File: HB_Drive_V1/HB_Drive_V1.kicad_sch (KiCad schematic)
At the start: 0 parts

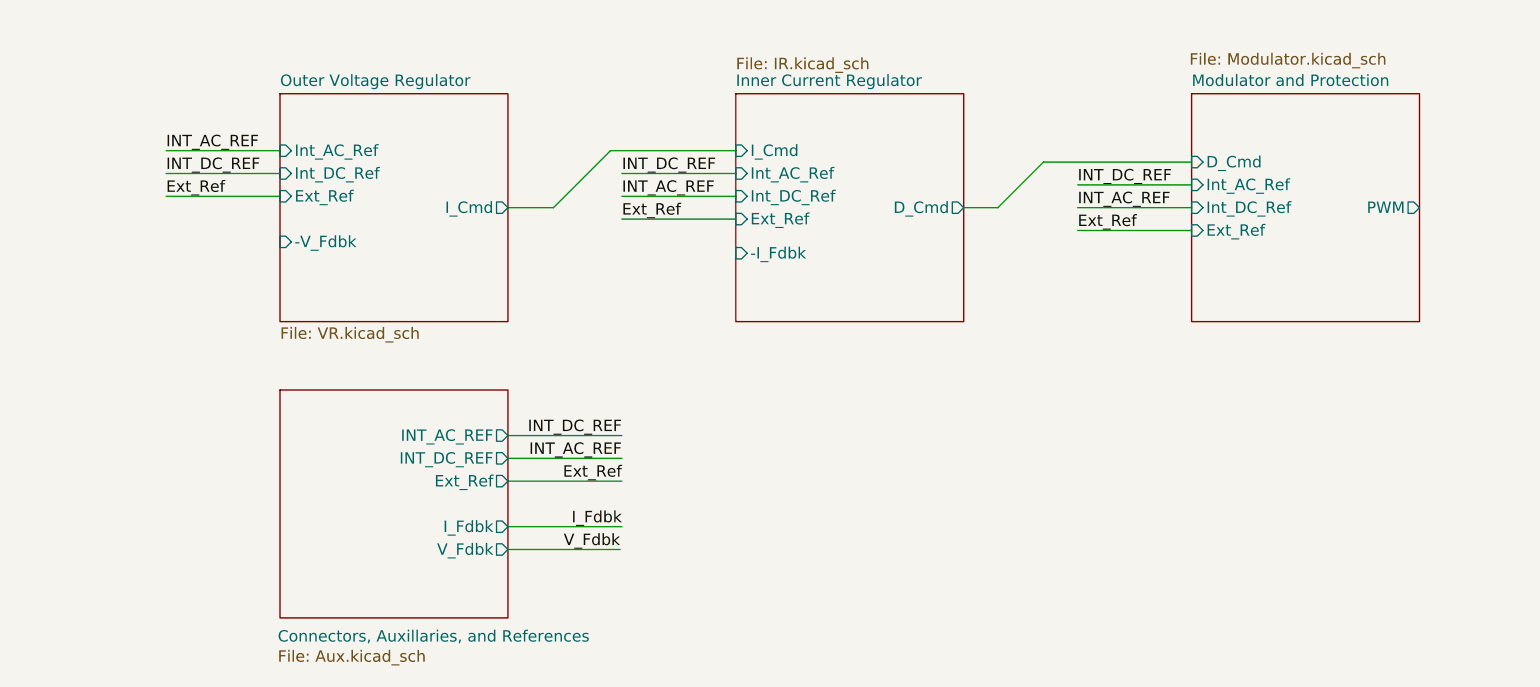
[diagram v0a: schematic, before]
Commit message: finishes hirearchical labels, add 10v +- ref generation and updates the DC offset circuits
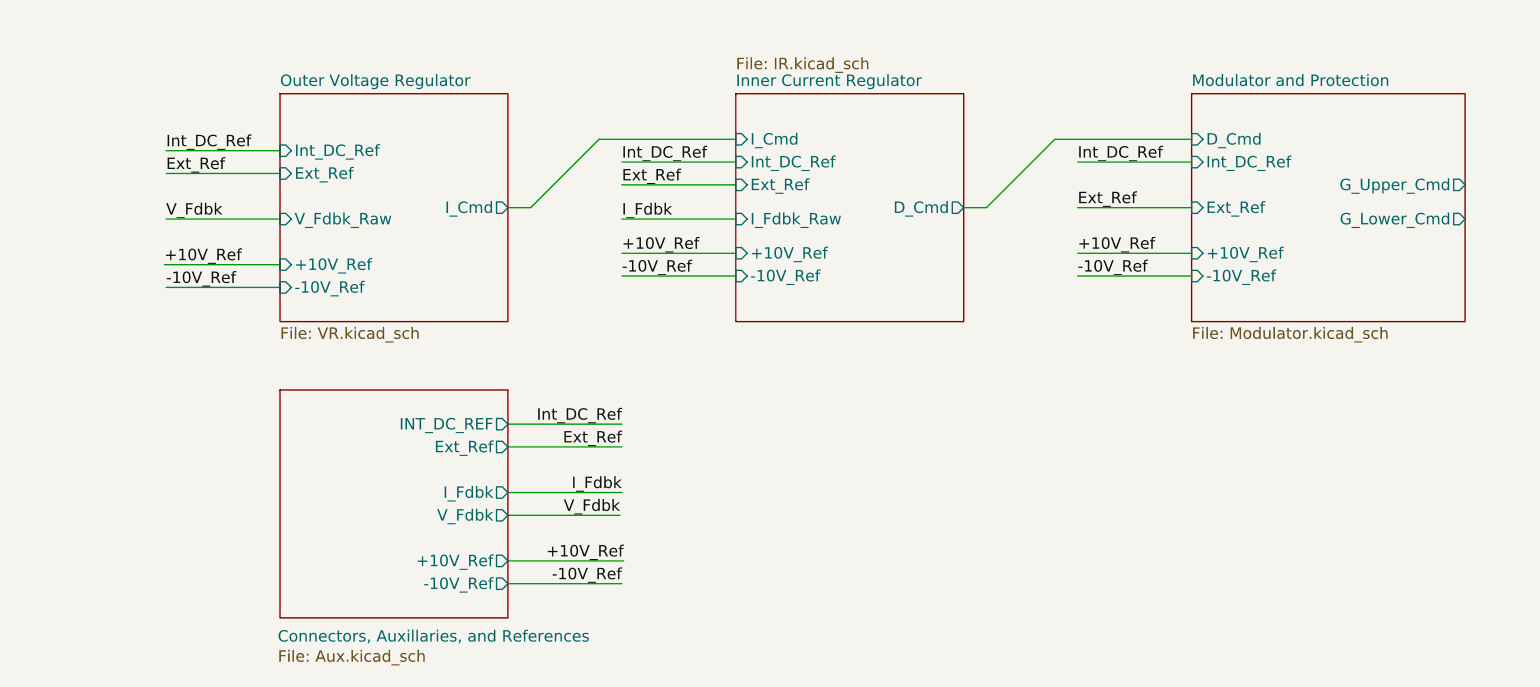
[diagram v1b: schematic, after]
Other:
- sheet Connectors, Auxillaries, and References ports: added +10V_Ref, -10V_Ref; removed INT_AC_REF
- sheet Inner Current Regulator ports: added +10V_Ref, -10V_Ref, I_Fdbk_Raw; removed -I_Fdbk, Int_AC_Ref
- sheet Modulator and Protection ports: added +10V_Ref, -10V_Ref, G_Lower_Cmd, G_Upper_Cmd; removed Int_AC_Ref, PWM
- sheet Outer Voltage Regulator ports: added +10V_Ref, -10V_Ref, V_Fdbk_Raw; removed -V_Fdbk, Int_AC_Ref

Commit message: updates board to highest working copy
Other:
- sheet Connectors, Auxillaries, and References ports: added Ext_Cmd, G_Lower_Cmd, G_Upper_Cmd, I_Fdbk_Raw, Int_Cmd, V_Fdbk_Raw; removed Ext_Ref, INT_DC_REF, I_Fdbk, V_Fdbk
- sheet Inner Current Regulator ports: added Ext_Cmd, Int_Cmd; removed Ext_Ref, Int_DC_Ref
- sheet Modulator and Protection ports: added Ext_Cmd, I_Fdbk_Raw, Int_Cmd; removed Ext_Ref, Int_DC_Ref
- sheet Outer Voltage Regulator ports: added Ext_Cmd, Int_Cmd; removed Ext_Ref, Int_DC_Ref

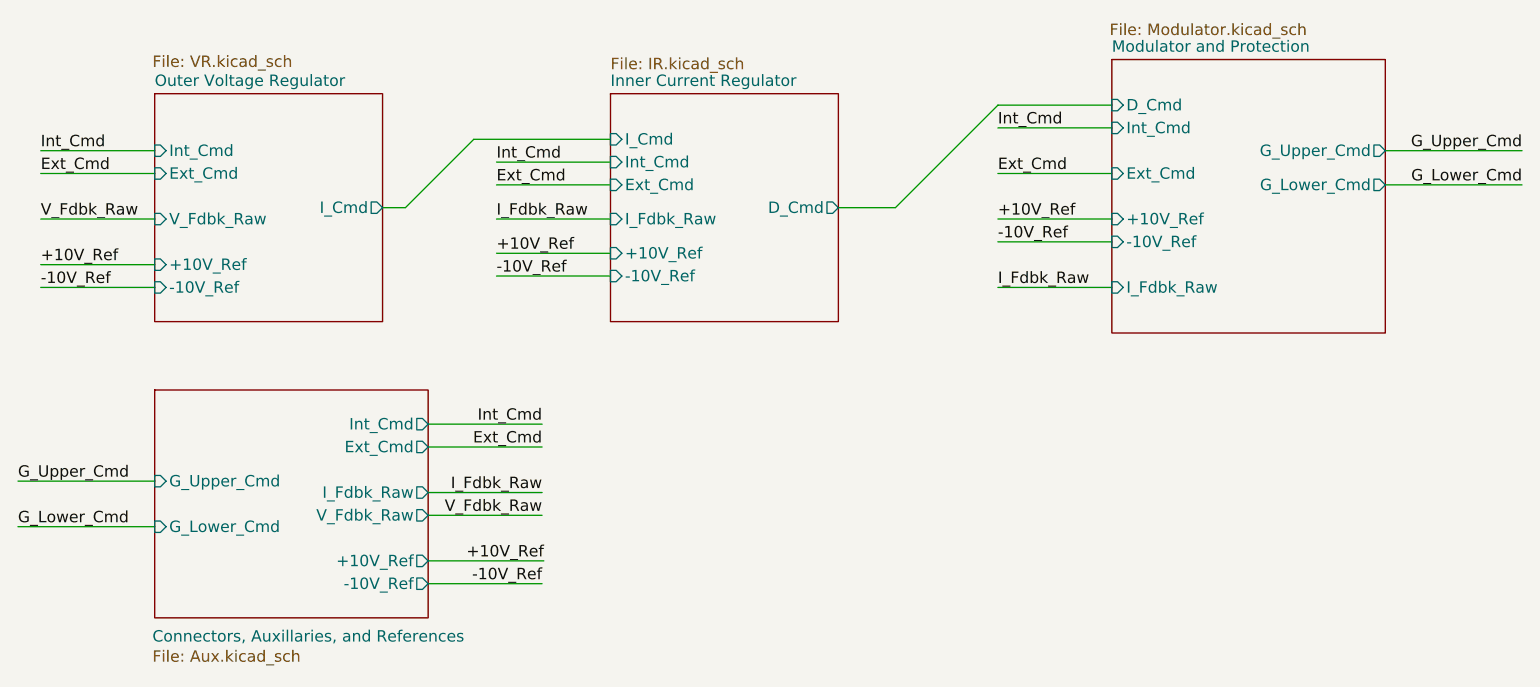
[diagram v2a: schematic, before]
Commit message: removes Aux file trouble
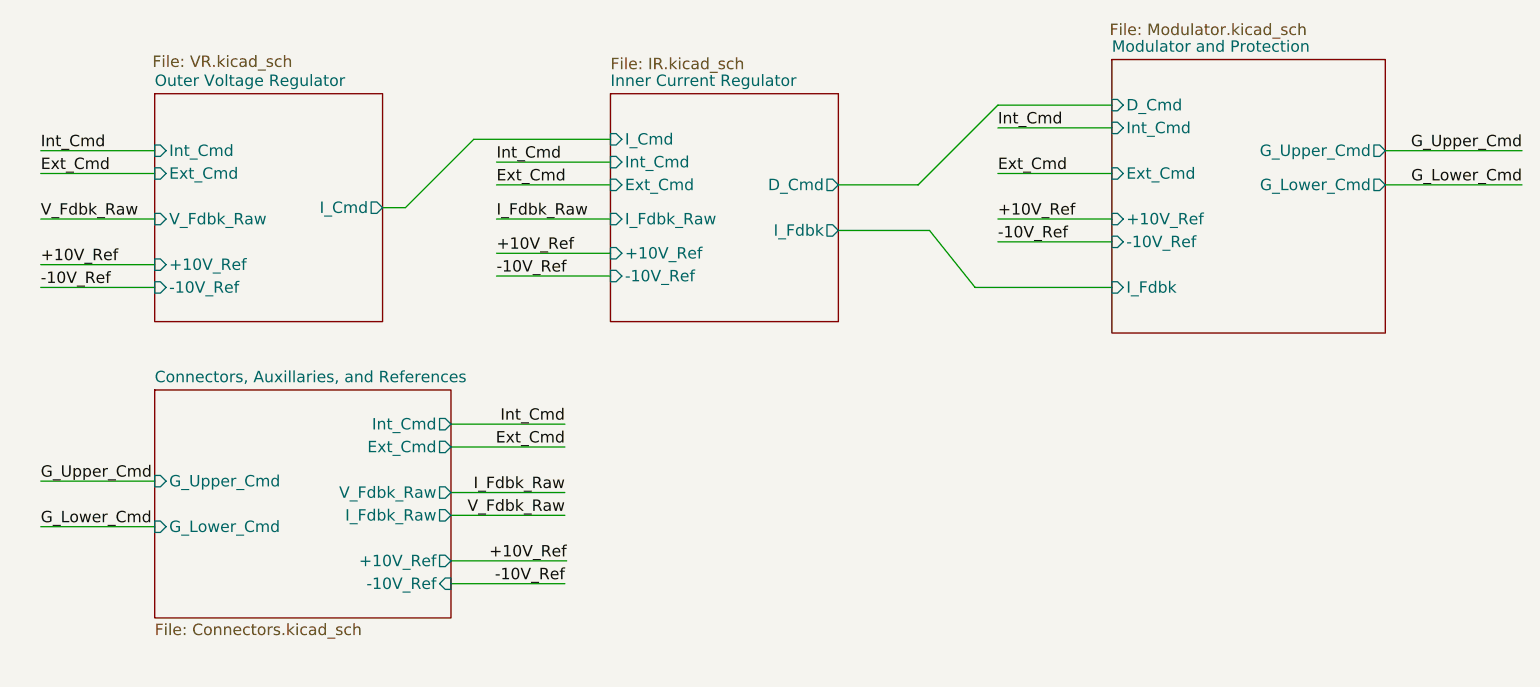
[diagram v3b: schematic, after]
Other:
- sheet Connectors, Auxillaries, and References: file Aux.kicad_sch -> Connectors.kicad_sch
- sheet Inner Current Regulator ports: added I_Fdbk; removed none
- sheet Modulator and Protection ports: added I_Fdbk; removed I_Fdbk_Raw
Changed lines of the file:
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@@
 	(wire
 		(pts
-			(xy 105.41 123.19) (xy 118.11 123.19)
-		)
-		(stroke
-			(width 0)
-			(type default)
-		)
-	)
-	(wire
-		(pts
-			(xy 105.41 115.57) (xy 118.11 115.57)
-		)
-		(stroke
-			(width 0)
-			(type default)
-		)
-	)
-	(wire
-		(pts
-			(xy 118.11 113.03) (xy 105.41 113.03)
-		)
-		(stroke
-			(width 0)
-			(type default)
-		)
-	)
-	(wire
-		(pts
-			(xy 59.69 111.76) (xy 74.93 111.76)
+			(xy 107.95 123.19) (xy 120.65 123.19)
+		)
+		(stroke
+			(width 0)
+			(type default)
+		)
+	)
+	(wire
+		(pts
+			(xy 107.95 115.57) (xy 120.65 115.57)
+		)
+		(stroke
+			(width 0)
+			(type default)
+		)
+	)
+	(wire
+		(pts
+			(xy 120.65 113.03) (xy 107.95 113.03)
+		)
+		(stroke
+			(width 0)
+			(type default)
+		)
+	)
+	(wire
+		(pts
+			(xy 62.23 111.76) (xy 74.93 111.76)
 		)
 		(stroke
@@
 	(wire
 		(pts
+			(xy 166.37 90.17) (xy 161.29 83.82)
+		)
+		(stroke
+			(width 0)
+			(type default)
+		)
+	)
+	(wire
+		(pts
+			(xy 151.13 83.82) (xy 161.29 83.82)
+		)
+		(stroke
+			(width 0)
+			(type default)
+		)
+	)
+	(wire
+		(pts
 			(xy 168.91 69.85) (xy 181.61 69.85)
 		)
@@
 	(wire
 		(pts
-			(xy 59.69 116.84) (xy 74.93 116.84)
+			(xy 62.23 116.84) (xy 74.93 116.84)
+		)
+		(stroke
+			(width 0)
+			(type default)
+		)
+	)
+	(wire
+		(pts
+			(xy 151.13 78.74) (xy 160.02 78.74)
 		)
 		(stroke
@@
 	(wire
 		(pts
-			(xy 118.11 105.41) (xy 105.41 105.41)
-		)
-		(stroke
-			(width 0)
-			(type default)
-		)
-	)
-	(wire
-		(pts
-			(xy 151.13 81.28) (xy 157.48 81.28)
+			(xy 120.65 105.41) (xy 107.95 105.41)
+		)
+		(stroke
+			(width 0)
+			(type default)
+		)
+	)
+	(wire
+		(pts
+			(xy 181.61 90.17) (xy 166.37 90.17)
 		)
 		(stroke
@@
 	(wire
 		(pts
-			(xy 105.41 120.65) (xy 118.308 120.65)
+			(xy 107.95 120.65) (xy 120.848 120.65)
 		)
 		(stroke
@@
 	(wire
 		(pts
-			(xy 157.48 81.28) (xy 168.91 69.85)
-		)
-		(stroke
-			(width 0)
-			(type default)
-		)
-	)
-	(wire
-		(pts
-			(xy 118.11 107.95) (xy 105.41 107.95)
-		)
-		(stroke
-			(width 0)
-			(type default)
-		)
-	)
-	(wire
-		(pts
-			(xy 168.91 90.17) (xy 181.61 90.17)
+			(xy 160.02 78.74) (xy 168.91 69.85)
+		)
+		(stroke
+			(width 0)
+			(type default)
+		)
+	)
+	(wire
+		(pts
+			(xy 120.65 107.95) (xy 107.95 107.95)
 		)
 		(stroke
@@
 	)
 	(label "V_Fdbk_Raw"
-		(at 118.11 115.57 180)
+		(at 120.65 115.57 180)
 		(effects
 			(font
@@
 	)
 	(label "G_Lower_Cmd"
-		(at 59.69 116.84 0)
+		(at 62.23 116.84 0)
 		(effects
 			(font
@@
 	)
 	(label "-10V_Ref"
-		(at 118.11 123.19 180)
+		(at 120.65 123.19 180)
 		(effects
 			(font
@@
 			)
 			(justify right bottom)
-		)
-	)
-	(label "I_Fdbk_Raw"
-		(at 168.91 90.17 0)
-		(effects
-			(font
-				(size 1.27 1.27)
-			)
-			(justify left bottom)
 		)
 	)
@@
 	)
 	(label "Int_Cmd"
-		(at 118.11 105.41 180)
+		(at 120.65 105.41 180)
 		(effects
 			(font
@@
 	)
 	(label "G_Upper_Cmd"
-		(at 59.69 111.76 0)
+		(at 62.23 111.76 0)
 		(effects
 			(font
@@
 	)
 	(label "+10V_Ref"
-		(at 118.308 120.65 180)
+		(at 120.848 120.65 180)
 		(effects
 			(font
@@
 	)
 	(label "I_Fdbk_Raw"
-		(at 118.11 113.03 180)
+		(at 120.65 113.03 180)
 		(effects
 			(font
@@
 	)
 	(label "Ext_Cmd"
-		(at 118.11 107.95 180)
+		(at 120.65 107.95 180)
 		(effects
 			(font
@@
 			)
 		)
-		(pin "I_Fdbk_Raw" input
+		(pin "I_Fdbk" input
 			(at 181.61 90.17 180)
 			(effects
@@
 		)
 		(pin "D_Cmd" output
-			(at 151.13 81.28 0)
+			(at 151.13 78.74 0)
 			(effects
 				(font
@@
 				)
 				(justify left)
+			)
+		)
+		(pin "I_Fdbk" output
+			(at 151.13 83.82 0)
+			(effects
+				(font
+					(size 1.27 1.27)
+				)
+				(justify right)
 			)
 		)
@@
 	(sheet
 		(at 74.93 101.6)
-		(size 30.48 25.4)
+		(size 33.02 25.4)
 		(exclude_from_sim no)
 		(in_bom yes)
 		(on_board yes)
 		(dnp no)
+		(fields_autoplaced yes)
 		(stroke
 			(width 0.1524)
@@
 		)
 		(property "Sheetname" "Connectors, Auxillaries, and References"
-			(at 74.676 129.794 0)
+			(at 74.93 100.8884 0)
 			(show_name no)
 			(do_not_autoplace no)
@@
 			)
 		)
-		(property "Sheetfile" "Aux.kicad_sch"
-			(at 74.676 130.556 0)
+		(property "Sheetfile" "Connectors.kicad_sch"
+			(at 74.93 127.5846 0)
 			(show_name no)
 			(do_not_autoplace no)
@@
 			)
 		)
+		(pin "+10V_Ref" output
+			(at 107.95 120.65 0)
+			(effects
+				(font
+					(size 1.27 1.27)
+				)
+				(justify right)
+			)
+		)
+		(pin "-10V_Ref" input
+			(at 107.95 123.19 0)
+			(effects
+				(font
+					(size 1.27 1.27)
+				)
+				(justify right)
+			)
+		)
 		(pin "Ext_Cmd" output
-			(at 105.41 107.95 0)
-			(effects
-				(font
-					(size 1.27 1.27)
-				)
-				(justify right)
-			)
-		)
-		(pin "+10V_Ref" output
-			(at 105.41 120.65 0)
-			(effects
-				(font
-					(size 1.27 1.27)
-				)
-				(justify right)
-			)
-		)
-		(pin "-10V_Ref" output
-			(at 105.41 123.19 0)
-			(effects
-				(font
-					(size 1.27 1.27)
-				)
-				(justify right)
-			)
-		)
-		(pin "I_Fdbk_Raw" output
-			(at 105.41 113.03 0)
-			(effects
-				(font
-					(size 1.27 1.27)
-				)
-				(justify right)
-			)
-		)
-		(pin "V_Fdbk_Raw" output
-			(at 105.41 115.57 0)
+			(at 107.95 107.95 0)
 			(effects
 				(font
@@
 		)
 		(pin "Int_Cmd" output
-			(at 105.41 105.41 0)
+			(at 107.95 105.41 0)
+			(effects
+				(font
+					(size 1.27 1.27)
+				)
+				(justify right)
+			)
+		)
+		(pin "I_Fdbk_Raw" output
+			(at 107.95 115.57 0)
+			(effects
+				(font
+					(size 1.27 1.27)
+				)
+				(justify right)
+			)
+		)
+		(pin "V_Fdbk_Raw" output
+			(at 107.95 113.03 0)
 			(effects
 				(font
@@
 			(project "HB_Drive_V1"
 				(path "/a9b54c89-4c8e-4c90-8a0d-ec2009e369b7"
-					(page "9")
-				)
-			)
+					(page "5")
+				)
+			)

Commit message: Annotates Schematic! Fixes REV1 wiring swaps and replaces buffer
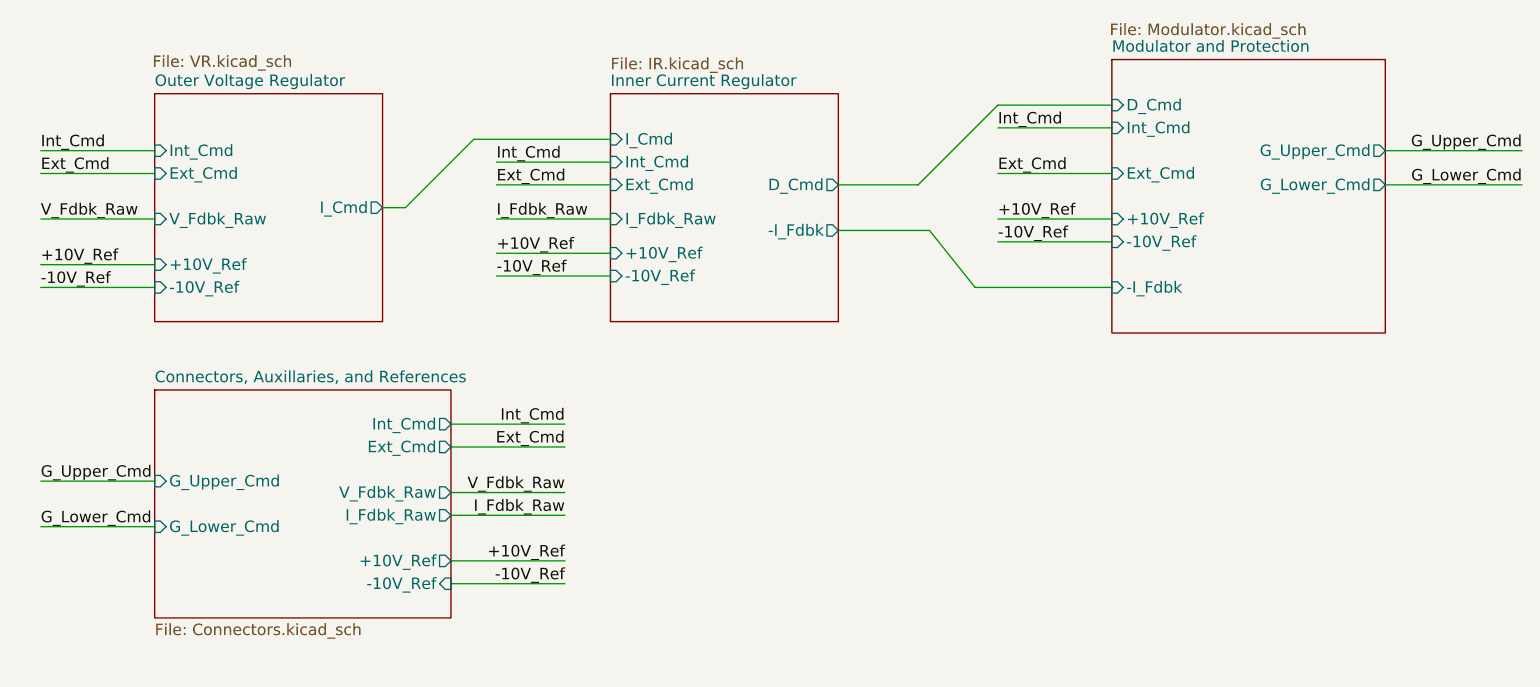
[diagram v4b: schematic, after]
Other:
- sheet Inner Current Regulator ports: added -I_Fdbk; removed I_Fdbk
- sheet Modulator and Protection ports: added -I_Fdbk; removed I_Fdbk
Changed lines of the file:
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@@
 	(wire
 		(pts
-			(xy 107.95 120.65) (xy 120.848 120.65)
+			(xy 107.95 120.65) (xy 120.65 120.65)
 		)
 		(stroke
@@
 			(width 0)
 			(type default)
-		)
-	)
-	(label "V_Fdbk_Raw"
-		(at 120.65 115.57 180)
-		(effects
-			(font
-				(size 1.27 1.27)
-			)
-			(justify right bottom)
 		)
 	)
@@
 		)
 	)
+	(label "V_Fdbk_Raw"
+		(at 120.65 113.03 180)
+		(effects
+			(font
+				(size 1.27 1.27)
+			)
+			(justify right bottom)
+		)
+	)
 	(label "-10V_Ref"
 		(at 120.65 123.19 180)
@@
 	)
 	(label "+10V_Ref"
-		(at 120.848 120.65 180)
+		(at 120.65 120.65 180)
+		(effects
+			(font
+				(size 1.27 1.27)
+			)
+			(justify right bottom)
+		)
+	)
+	(label "I_Fdbk_Raw"
+		(at 120.65 115.57 180)
 		(effects
 			(font
@@
 			)
 			(justify left bottom)
-		)
-	)
-	(label "I_Fdbk_Raw"
-		(at 120.65 113.03 180)
-		(effects
-			(font
-				(size 1.27 1.27)
-			)
-			(justify right bottom)
 		)
 	)
@@
 			)
 		)
-		(pin "I_Fdbk" input
+		(pin "-I_Fdbk" input
 			(at 181.61 90.17 180)
 			(effects
@@
 			)
 		)
-		(pin "I_Fdbk" output
+		(pin "-I_Fdbk" output
 			(at 151.13 83.82 0)
 			(effects

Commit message: Brings everything up to latest copy on my computer
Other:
- company: (none) -> UW Madison, WEMPEC
- title: (none) -> HB Drive V3
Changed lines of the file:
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@@
 	(generator_version "10.0")
 	(paper "A4")
+	(title_block
+		(title "HB Drive V3")
+		(date "2026-09-08")
+		(company "UW Madison, WEMPEC")
+	)
 	(wire
 		(pts
@@
 	)
 	(embedded_fonts no)
+	(embedded_files
+		(file
+			(name "HB_Drive_DrawingSheet.kicad_wks")
+			(type worksheet)
+			(data |KLUv/WBSCfUTADadWyAQlxsmHCQ5WsE9iJiZqcm/BSUXGHAP2Jd8kB0RALwI0FIASgBVAI83EP/H
+				Y3OUfa0n14/zHfcMVFqxP99Zkl/rGagl2082/JJ/AQAICEDRexitKCtOZTvneGDVGX/Nft1juKSU
+				iBlnX2zD7KMCICAIQyROVzkbKgT+29OIoLMjNZUyd21/ddA7Zr8Zc+917FiFOOxt7d7bb/98d1eE
+				c+2q//r3YS7GaM2e3V2fM1ILm41dmIVF2Z/rh1XV/tX7nOcPf265rqoh0ko0FuWEol0smYbzaDg0
+				CIpALWrRjlJilqIXVyrDNB6cLHO5aChCM/zrI+dsyv7XuTZ17IciEJ0tG6ZJO27bFiWiAPiLO7Lp
+				7BCDlaz6SwEBgWEqJsUQi8RMIKScM14SM8kkplvBDzvoZtKoSCgOznr1bRtmz4UVZRbBaBjvLWbK
+				KTvb7/65DA6pQadV/fXLuNPZwVqxZJVG5WQvnYe3TkxNk1lGAXag0USHGBoSEUmSJB1wRKTmyDbc
+				ROt80O/+GLIOvXLR7DGm3REmE+8KO2aYNRgksHbMKBDLzdUygFUuAjKiX4pxbop5Fx1LeOqr5PRh
+				sOe58AfJfJDBPYcs1ASWtgmA+AgMfYw728vPWSuH8xgXQ5k8LWCCsE/cFQQtAfI0EZpeSlNMlo5T
+				t/MB93OmLRzQzD9Pz+owQkdMvGhUsmYhj43lEvkaQE8t/eGBEM0h/UVjJe/OcYC8P+d52ECQCYQl
+				WnTmaw9Q29Tm0yQIaFaVpNSgrSa9kAeCOdE9K3yyxNgk0L/6NETFfHYaJHe26EZKC5LyG5FATvGI
+				YYkGbXq+RhzrA8FyEbeRiwb4Y9Cr|
+			)
+			(checksum "B515CD35CD4FAC14689C7CE4AC7D9023")
+		)
+	)
 )
